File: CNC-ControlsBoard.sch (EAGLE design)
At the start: 42 parts, among them IC1 ATTINY84-20PU, IC2 MAX7219CNG, IC3 74HCT4053P, IC4 74HCT165N, IC5 74HCT165N, IC6 74HCT157N, IC7 74HC148N

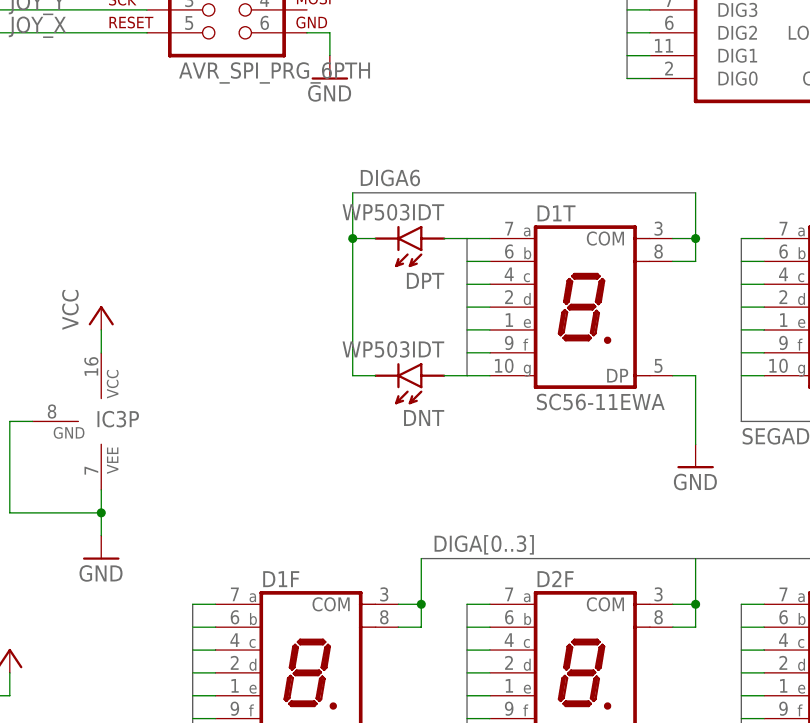
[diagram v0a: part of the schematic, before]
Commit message: Housekeeping: - deleted obsolete Interface and Main -only boards and schematics. All these have been condensed in the MainStepInterface panel now - updated .gitignore to include library backups - updated symbol of 7-segment display to make it smaller - minor touch-ups on Controls PCB
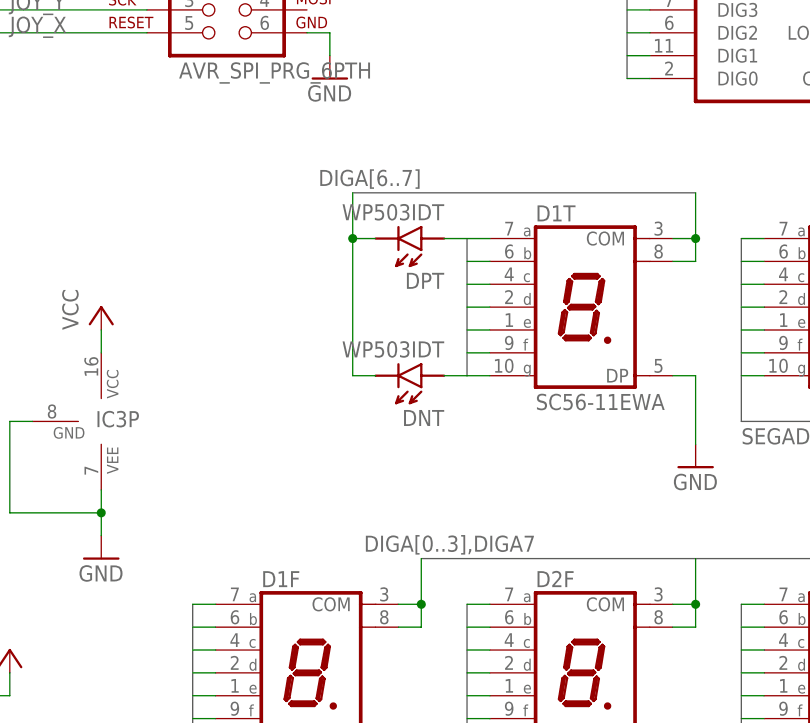
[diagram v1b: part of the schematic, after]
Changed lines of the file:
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@@
 <?xml version="1.0" encoding="utf-8"?>
 <!DOCTYPE eagle SYSTEM "eagle.dtd">
-<eagle version="6.3">
+<eagle version="6.4">
 <drawing>
 <settings>
@@
 </segment>
 </bus>
-<bus name="SEGDA,SEGDB,SEGDC,SEGDD,SEGDE,SEGDF,SEGDG,SEGDDP,SRE7,SRF0">
+<bus name="SEGAA,SEGAB,SEGAC,SEGAD,SEGAE,SEGAF,SEGAG,SEGADP">
 <segment>
 <wire x1="114.3" y1="73.66" x2="114.3" y2="58.42" width="0.762" layer="92"/>
 </segment>
 </bus>
-<bus name="DIGA6">
+<bus name="DIGA[6..7]">
 <segment>
 <wire x1="101.6" y1="78.74" x2="139.7" y2="78.74" width="0.762" layer="92"/>
@@
 </segment>
 </bus>
-<bus name="DIGA[0..3]">
+<bus name="DIGA[0..3],DIGA7">
 <segment>
 <wire x1="109.22" y1="38.1" x2="205.74" y2="38.1" width="0.762" layer="92"/>

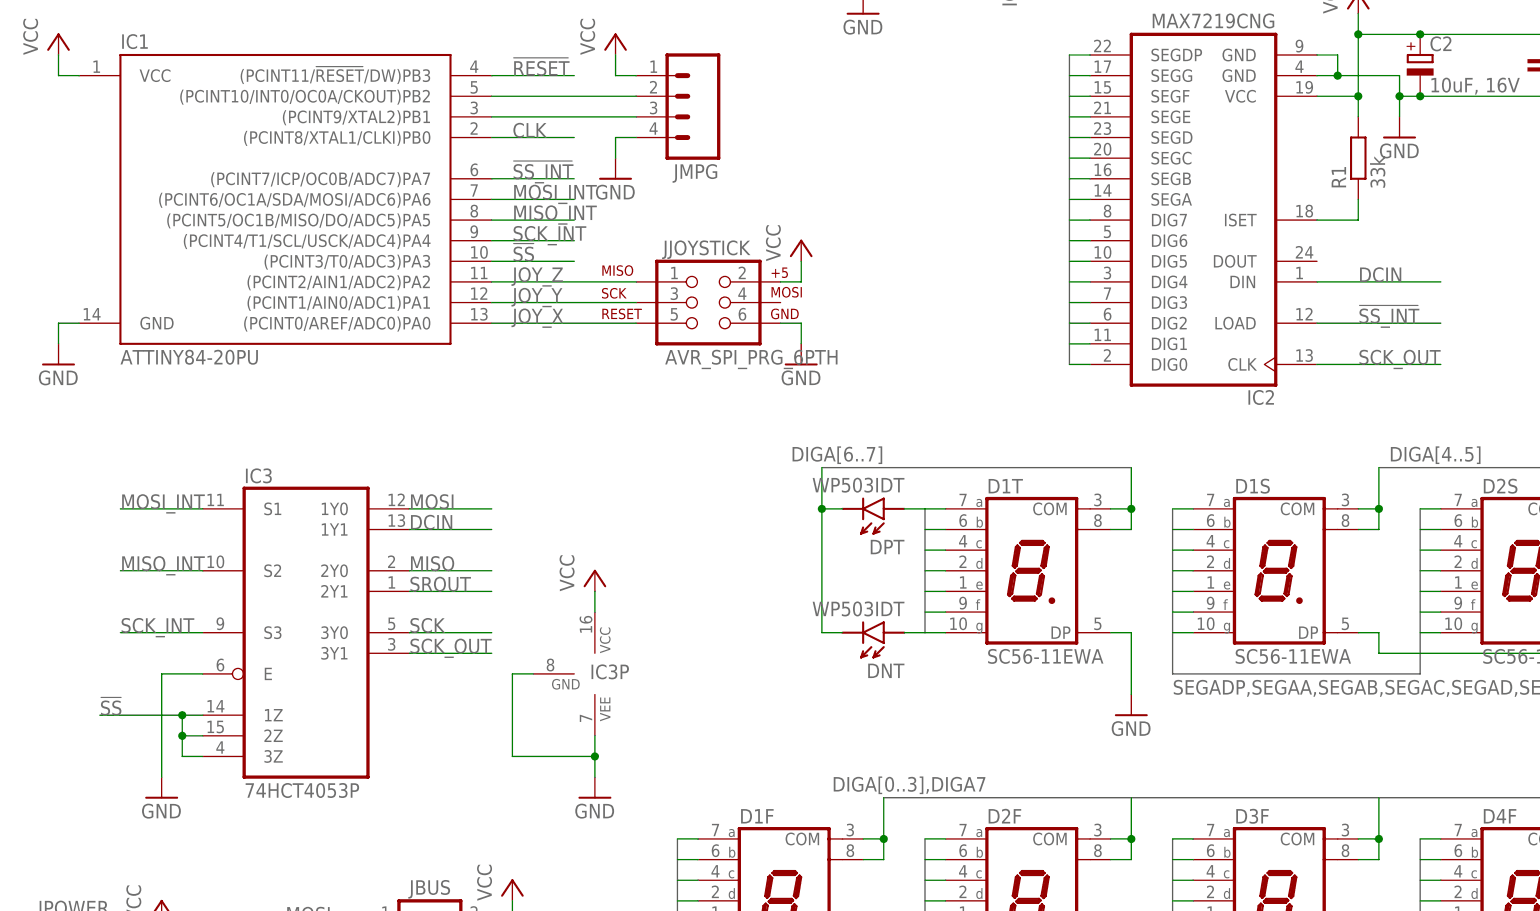
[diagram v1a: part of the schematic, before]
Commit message: BUGFIX: Same 4053 mistake fixed on Controls board as well UPDATE: 27k instead of 33k for Riset as all LEDs can handle 20mA at 2.1V - routed both DRO and Controls in FreeRouting - updated silkscreen/artwork to reflect new revision - still needs to fix DRU checks (FreeRouting always sees non-PTH holes smaller)
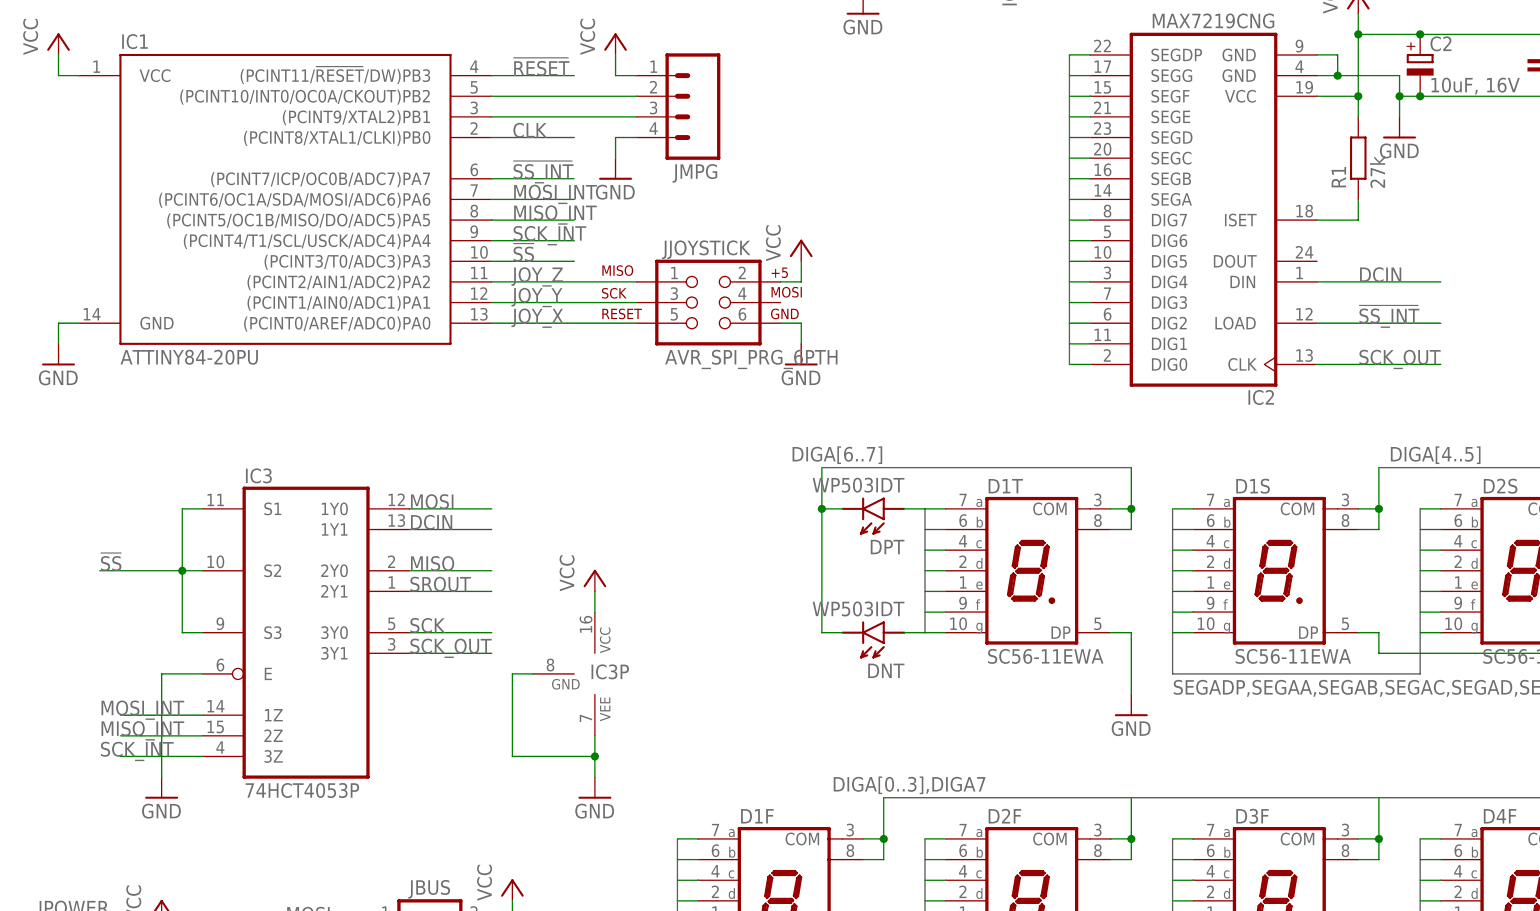
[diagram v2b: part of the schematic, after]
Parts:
- R1: value 33k -> 27k
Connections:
- net !SS: now also IC3G$1.S1, IC3G$1.S2, IC3G$1.S3; no longer IC3G$1.1Z, IC3G$1.2Z, IC3G$1.3Z
- net MISO_INT: now also IC3G$1.2Z; no longer IC3G$1.S2
- net MOSI_INT: now also IC3G$1.1Z; no longer IC3G$1.S1
- net SCK_INT: now also IC3G$1.3Z; no longer IC3G$1.S3
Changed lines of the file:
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@@
 <setting verticaltext="up"/>
 </settings>
-<grid distance="0.1" unitdist="inch" unit="inch" style="lines" multiple="1" display="no" altdistance="0.01" altunitdist="inch" altunit="inch"/>
+<grid distance="0.1" unitdist="inch" unit="inch" style="lines" multiple="1" display="yes" altdistance="0.01" altunitdist="inch" altunit="inch"/>
 <layers>
 <layer number="1" name="Top" color="4" fill="1" visible="no" active="no"/>
@@
 <part name="GND1" library="supply1" deviceset="GND" device=""/>
 <part name="IC2" library="maxim" deviceset="MAX7219CNG" device=""/>
-<part name="R1" library="rcl" deviceset="R-EU_" device="0207/10" value="33k"/>
+<part name="R1" library="rcl" deviceset="R-EU_" device="0207/10" value="27k"/>
 <part name="+5V" library="supply1" deviceset="VCC" device=""/>
 <part name="C1" library="rcl" deviceset="C-EU" device="050-025X075" value="100nF, 63V"/>
@@
 </segment>
 <segment>
-<pinref part="IC3" gate="G$1" pin="1Z"/>
-<wire x1="12.7" y1="48.26" x2="22.86" y2="48.26" width="0.1524" layer="91"/>
-<wire x1="22.86" y1="48.26" x2="25.4" y2="48.26" width="0.1524" layer="91"/>
-<wire x1="22.86" y1="48.26" x2="22.86" y2="45.72" width="0.1524" layer="91"/>
-<junction x="22.86" y="48.26"/>
-<pinref part="IC3" gate="G$1" pin="3Z"/>
-<wire x1="22.86" y1="45.72" x2="22.86" y2="43.18" width="0.1524" layer="91"/>
-<wire x1="22.86" y1="43.18" x2="25.4" y2="43.18" width="0.1524" layer="91"/>
-<pinref part="IC3" gate="G$1" pin="2Z"/>
-<wire x1="25.4" y1="45.72" x2="22.86" y2="45.72" width="0.1524" layer="91"/>
-<junction x="22.86" y="45.72"/>
-<label x="12.7" y="48.26" size="1.778" layer="95"/>
+<wire x1="12.7" y1="66.04" x2="22.86" y2="66.04" width="0.1524" layer="91"/>
+<label x="12.7" y="66.04" size="1.778" layer="95"/>
+<pinref part="IC3" gate="G$1" pin="S2"/>
+<wire x1="25.4" y1="66.04" x2="22.86" y2="66.04" width="0.1524" layer="91"/>
+<pinref part="IC3" gate="G$1" pin="S1"/>
+<wire x1="25.4" y1="73.66" x2="22.86" y2="73.66" width="0.1524" layer="91"/>
+<wire x1="22.86" y1="73.66" x2="22.86" y2="66.04" width="0.1524" layer="91"/>
+<junction x="22.86" y="66.04"/>
+<wire x1="22.86" y1="66.04" x2="22.86" y2="58.42" width="0.1524" layer="91"/>
+<pinref part="IC3" gate="G$1" pin="S3"/>
+<wire x1="22.86" y1="58.42" x2="25.4" y2="58.42" width="0.1524" layer="91"/>
 </segment>
 </net>
@@
 </segment>
 <segment>
-<pinref part="IC3" gate="G$1" pin="S3"/>
-<wire x1="25.4" y1="58.42" x2="15.24" y2="58.42" width="0.1524" layer="91"/>
-<label x="15.24" y="58.42" size="1.778" layer="95"/>
+<wire x1="17.78" y1="43.18" x2="15.24" y2="43.18" width="0.1524" layer="91"/>
+<label x="12.7" y="43.18" size="1.778" layer="95"/>
+<pinref part="IC3" gate="G$1" pin="3Z"/>
+<wire x1="25.4" y1="43.18" x2="17.78" y2="43.18" width="0.1524" layer="91"/>
 </segment>
 </net>
@@
 </segment>
 <segment>
-<pinref part="IC3" gate="G$1" pin="S1"/>
-<wire x1="25.4" y1="73.66" x2="15.24" y2="73.66" width="0.1524" layer="91"/>
-<label x="15.24" y="73.66" size="1.778" layer="95"/>
+<label x="12.7" y="48.26" size="1.778" layer="95"/>
+<pinref part="IC3" gate="G$1" pin="1Z"/>
+<wire x1="15.24" y1="48.26" x2="25.4" y2="48.26" width="0.1524" layer="91"/>
 </segment>
 </net>
@@
 </segment>
 <segment>
-<pinref part="IC3" gate="G$1" pin="S2"/>
-<wire x1="25.4" y1="66.04" x2="15.24" y2="66.04" width="0.1524" layer="91"/>
-<label x="15.24" y="66.04" size="1.778" layer="95"/>
-</segment>
-</net>
+<wire x1="17.78" y1="45.72" x2="15.24" y2="45.72" width="0.1524" layer="91"/>
+<label x="12.7" y="45.72" size="1.778" layer="95"/>
+<pinref part="IC3" gate="G$1" pin="2Z"/>
+<wire x1="17.78" y1="45.72" x2="25.4" y2="45.72" width="0.1524" layer="91"/>
+</segment>
+</net>
